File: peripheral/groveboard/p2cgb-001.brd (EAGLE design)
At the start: 91 x 55 mm, 8 parts

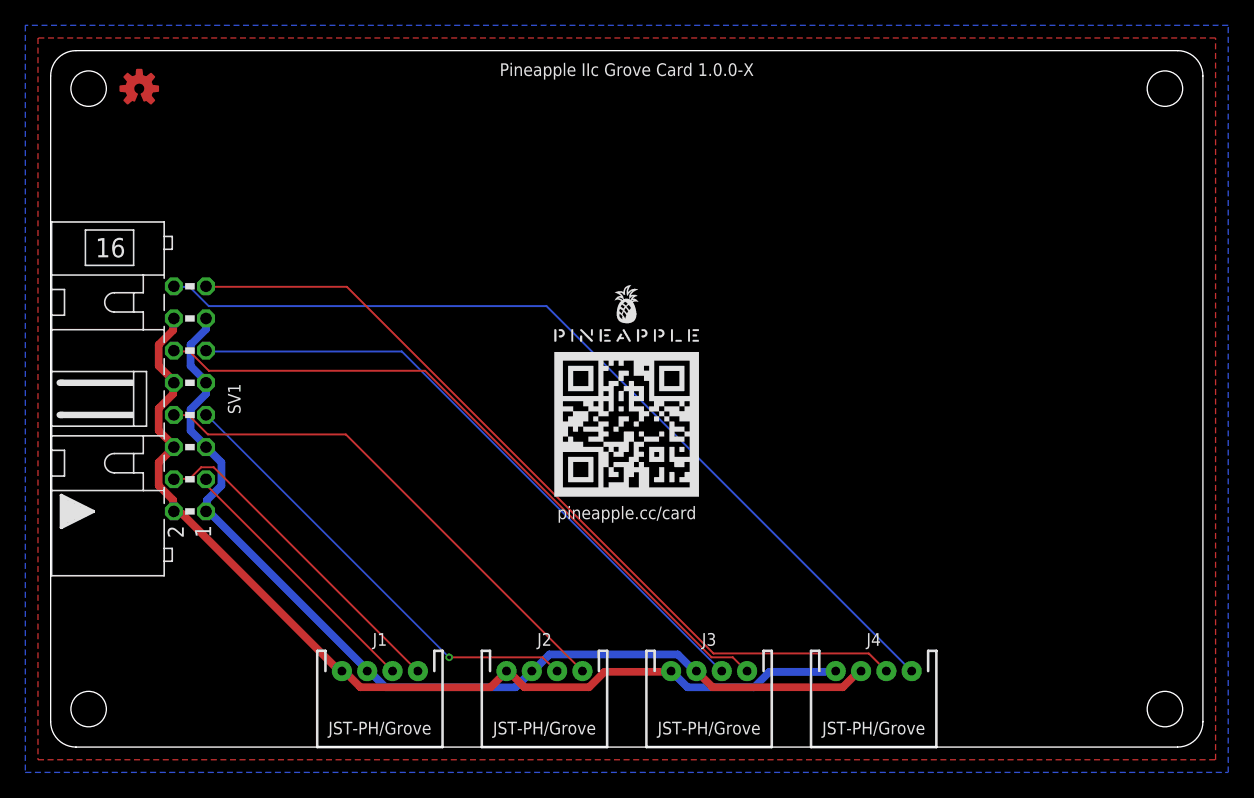
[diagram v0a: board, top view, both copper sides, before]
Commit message: Added bogopins to connect the logicboard and the groveboard.
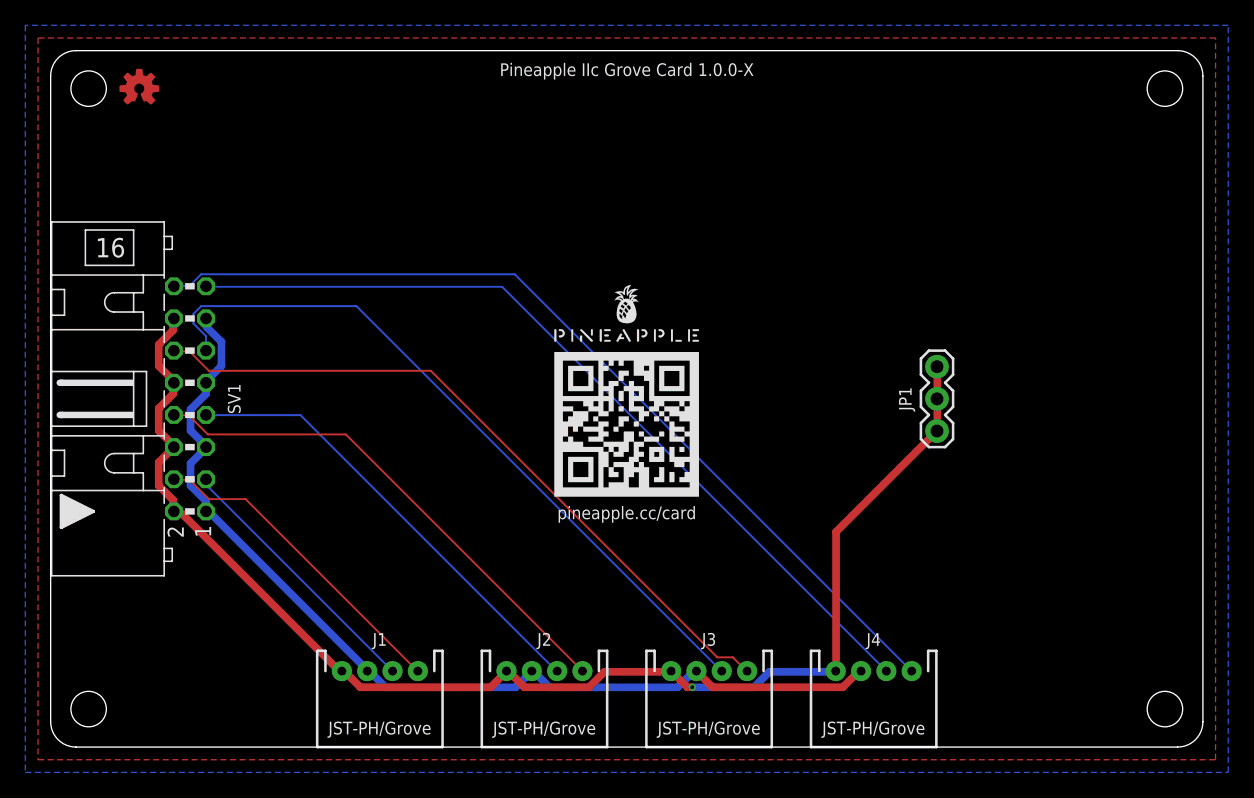
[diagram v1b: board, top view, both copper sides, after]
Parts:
- added JP1: (no value), SparkFun-Connectors:1X03
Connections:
- net GND: now also JP1.1, JP1.2, JP1.3
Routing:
- net GND: track 78.8 -> 106.2 mm, vias 0 -> 1
- net N$7: track 51.2 -> 57.2 mm
- net N$1: track 26.3 -> 25.5 mm
- net N$4: track 70.9 -> 71.6 mm
- net N$6: vias 1 -> 0
